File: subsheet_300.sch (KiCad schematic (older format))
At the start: 5 parts, among them U300_DIP40 ST_DMA_DIP40_PHY, U300_PLCC44 ST_DMA_PLCC44_PHY

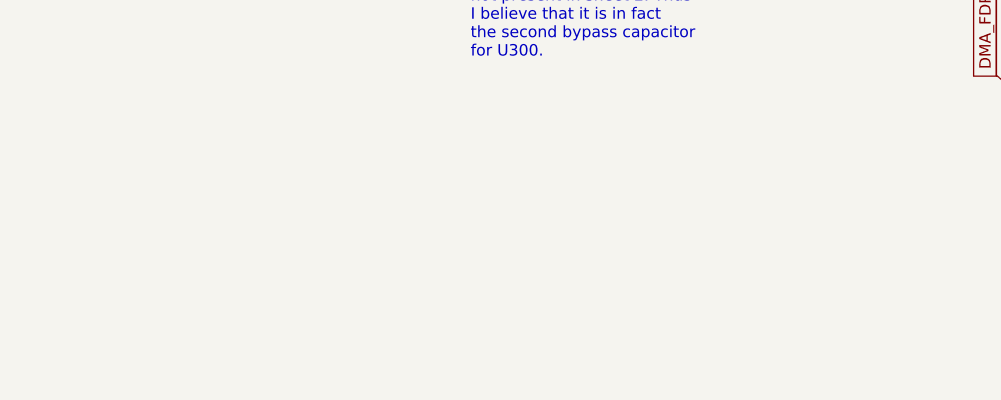
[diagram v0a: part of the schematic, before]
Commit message: Resolves #3 : Apply the DMA Pull up fix on databus
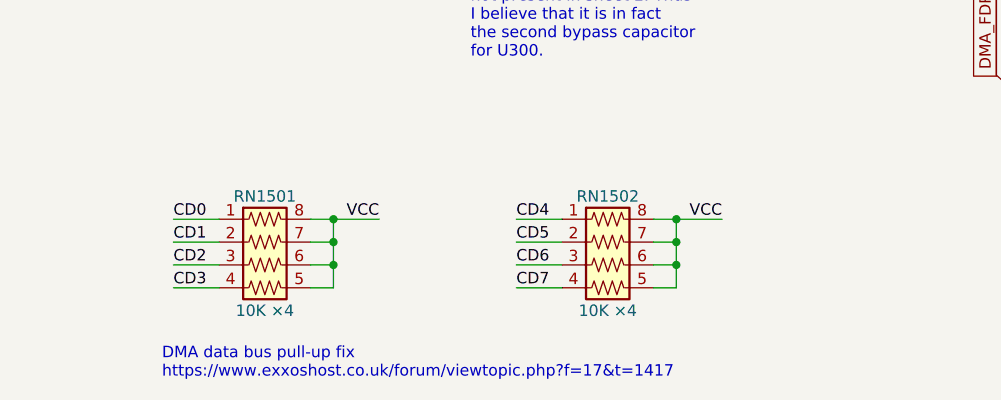
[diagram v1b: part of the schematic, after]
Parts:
- added RN1501, RN1502: 10K ×4, Resistor_SMD:R_Array_Convex_4x0603, symbol custom_passives:R_Pack04_US
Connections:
- net CD0: now also RN1501.1 (R1.1)
- net CD1: now also RN1501.2 (R2.1)
- net CD2: now also RN1501.3 (R3.1)
- net CD3: now also RN1501.4 (R4.1)
- net CD4: now also RN1502.1 (R1.1)
- net CD5: now also RN1502.2 (R2.1)
- net CD6: now also RN1502.3 (R3.1)
- net CD7: now also RN1502.4 (R4.1)
- net VCC: now also RN1501.5 (R4.2), RN1501.6 (R3.2), RN1501.7 (R2.2), RN1501.8 (R1.2), RN1502.5 (R4.2), RN1502.6 (R3.2), RN1502.7 (R2.2), RN1502.8 (R1.2)
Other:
- note added: "DMA data bus pull-up fix\nhttps://www.exxoshost.co.uk/forum/viewtopic.php?f=17&t=1417"
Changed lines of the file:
@@
 Wire Wire Line
 	3500 4650 3500 4850
+Wire Wire Line
+	2100 6000 2300 6000
+Wire Wire Line
+	2100 6300 2300 6300
+Wire Wire Line
+	2100 6200 2300 6200
+Wire Wire Line
+	2100 6100 2300 6100
+$Comp
+L custom_passives:R_Pack04_US RN?
+U 1 1 6206466E
+P 2500 6200
+AR Path="/6089D0C6/6206466E" Ref="RN?"  Part="1"
+AR Path="/60A1445F/6206466E" Ref="RN1501"  Part="1"
+F 0 "RN1501" V 2200 6200 50  0000 C CNN
+F 1 "10K ×4" V 2700 6200 50  0000 C CNN
+F 2 "Resistor_SMD:R_Array_Convex_4x0603" V 2775 6200 50  0001 C CNN
+F 3 "~" H 2500 6200 50  0001 C CNN
+	1    2500 6200
+	0    1    1    0
+$EndComp
+Text Label 3000 6000 2    50   ~ 0
+VCC
+Wire Wire Line
+	2700 6000 2800 6000
+Wire Wire Line
+	2700 6300 2800 6300
+Wire Wire Line
+	2800 6300 2800 6200
+Connection ~ 2800 6000
+Wire Wire Line
+	2800 6000 3000 6000
+Wire Wire Line
+	2700 6200 2800 6200
+Connection ~ 2800 6200
+Wire Wire Line
+	2800 6200 2800 6100
+Wire Wire Line
+	2700 6100 2800 6100
+Connection ~ 2800 6100
+Wire Wire Line
+	2800 6100 2800 6000
+Wire Wire Line
+	3600 6000 3800 6000
+Wire Wire Line
+	3600 6300 3800 6300
+Wire Wire Line
+	3600 6200 3800 6200
+Wire Wire Line
+	3600 6100 3800 6100
+$Comp
+L custom_passives:R_Pack04_US RN?
+U 1 1 6206AF44
+P 4000 6200
+AR Path="/6089D0C6/6206AF44" Ref="RN?"  Part="1"
+AR Path="/60A1445F/6206AF44" Ref="RN1502"  Part="1"
+F 0 "RN1502" V 3700 6200 50  0000 C CNN
+F 1 "10K ×4" V 4200 6200 50  0000 C CNN
+F 2 "Resistor_SMD:R_Array_Convex_4x0603" V 4275 6200 50  0001 C CNN
+F 3 "~" H 4000 6200 50  0001 C CNN
+	1    4000 6200
+	0    1    1    0
+$EndComp
+Text Label 4500 6000 2    50   ~ 0
+VCC
+Wire Wire Line
+	4200 6000 4300 6000
+Wire Wire Line
+	4200 6300 4300 6300
+Wire Wire Line
+	4300 6300 4300 6200
+Connection ~ 4300 6000
+Wire Wire Line
+	4300 6000 4500 6000
+Wire Wire Line
+	4200 6200 4300 6200
+Connection ~ 4300 6200
+Wire Wire Line
+	4300 6200 4300 6100
+Wire Wire Line
+	4200 6100 4300 6100
+Connection ~ 4300 6100
+Wire Wire Line
+	4300 6100 4300 6000
+Text Label 2100 6000 0    50   ~ 0
+CD0
+Text Label 2100 6100 0    50   ~ 0
+CD1
+Text Label 2100 6200 0    50   ~ 0
+CD2
+Text Label 2100 6300 0    50   ~ 0
+CD3
+Text Label 3600 6000 0    50   ~ 0
+CD4
+Text Label 3600 6100 0    50   ~ 0
+CD5
+Text Label 3600 6200 0    50   ~ 0
+CD6
+Text Label 3600 6300 0    50   ~ 0
+CD7
+Text Notes 2050 6700 0    50   ~ 0
+DMA data bus pull-up fix\nhttps://www.exxoshost.co.uk/forum/viewtopic.php?f=17&t=1417
 $EndSCHEMATC

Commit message: Resolves #13 : assign 1206 hand-solder footprints to resistors
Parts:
- R303: footprint commons_passives_THT:Passive_THT_resistor_W2.54mm_L12.70mm -> Resistor_SMD:R_1206_3216Metric_Pad1.30x1.75mm_HandSolder
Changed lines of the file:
@@
 F 0 "R303" V 4150 2000 50  0000 C CNN
 F 1 "1K" V 4350 2000 50  0000 C CNN
-F 2 "commons_passives_THT:Passive_THT_resistor_W2.54mm_L12.70mm" H 4250 2000 50  0001 C CNN
+F 2 "Resistor_SMD:R_1206_3216Metric_Pad1.30x1.75mm_HandSolder" H 4250 2000 50  0001 C CNN
 F 3 "~" H 4250 2000 50  0001 C CNN
 	1    4250 2000

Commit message: Resolves #8 : Assign 1206 hand-solder footprints to non polarized capacitors
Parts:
- C226, C302: footprint commons_passives_THT:Passive_THT_capacitor_mlcc_W2.54mm_L7.62mm -> Capacitor_SMD:C_1206_3216Metric_Pad1.33x1.80mm_HandSolder
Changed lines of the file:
@@
 F 0 "C302" H 3025 4600 50  0000 L CNN
 F 1 "0.1uF" H 3025 4400 50  0000 L CNN
-F 2 "commons_passives_THT:Passive_THT_capacitor_mlcc_W2.54mm_L7.62mm" H 3038 4350 50  0001 C CNN
+F 2 "Capacitor_SMD:C_1206_3216Metric_Pad1.33x1.80mm_HandSolder" H 3038 4350 50  0001 C CNN
 F 3 "~" H 3000 4500 50  0001 C CNN
 	1    3000 4500
@@
 F 0 "C226" H 3525 4600 50  0000 L CNN
 F 1 "0.1uF" H 3525 4400 50  0000 L CNN
-F 2 "commons_passives_THT:Passive_THT_capacitor_mlcc_W2.54mm_L7.62mm" H 3538 4350 50  0001 C CNN
+F 2 "Capacitor_SMD:C_1206_3216Metric_Pad1.33x1.80mm_HandSolder" H 3538 4350 50  0001 C CNN
 F 3 "~" H 3500 4500 50  0001 C CNN
 	1    3500 4500
